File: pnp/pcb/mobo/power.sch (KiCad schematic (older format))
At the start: 27 parts, among them J45 Jack-DC, U14 FDS4435BZ, U5 AP1117-33, U7 TPS54336ADDA

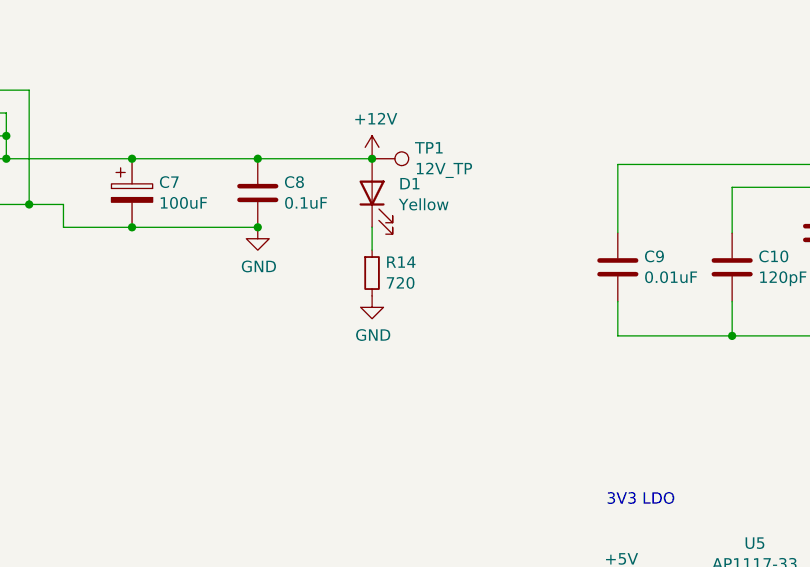
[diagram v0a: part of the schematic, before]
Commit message: - Fixing LED JLCPCB code to be a yellow LED as well as updating R14 to be 680R per Issue #99 - Updates to the schematic to include LCSC and JLC part numbers. - Updates to generate renders of the board as well as an HTML BOM with digikey links, and a JLCPCB BOM.
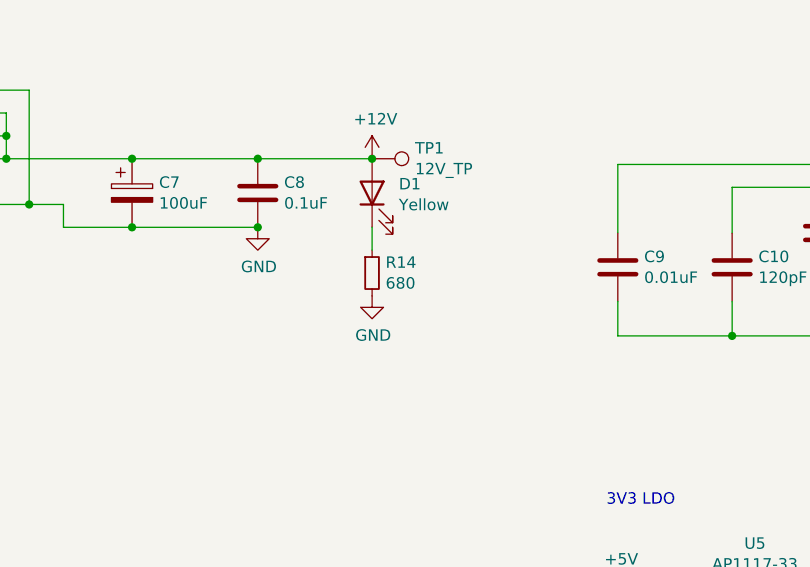
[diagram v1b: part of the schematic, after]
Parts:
- C10: Digikey (none) -> 399-1124-1-ND; JLCPCB (none) -> C159770; LCSC (none) -> C237175; Mouser (none) -> 80-C0805C121J5GAUTO
- C11, C9: Digikey (none) -> 1276-1015-1-ND; JLCPCB (none) -> C1710; LCSC (none) -> C83170; Mouser (none) -> 581-08055C104K
- C12, C29, C31, C8: Digikey (none) -> 1276-1180-1-ND; JLCPCB (none) -> C49678; LCSC (none) -> C360619; Mouser (none) -> 581-08055C104K
- C13, C30, C7: Digikey (none) -> 493-2203-1-ND; JLCPCB (none) -> C99837; LCSC (none) -> C263958; Mouser (none) -> 647-UWT1V101MCL1S
- D1, D2, D5: Digikey (none) -> 732-4987-1-ND; JLCPCB (none) -> C2296; LCSC (none) -> C779458; Mouser (none) -> 710-150080YS75000
- J45: LCSC (none) -> C16214
- L1: Digikey (none) -> SRR1260A-150MCT-ND; JLCPCB (none) -> C169395; LCSC (none) -> C397802; Mouser (none) -> 652-SRR1260A-150M
- R14: value 720 -> 680; JLCPCB (none) -> C17798; LCSC (none) -> C139848
- R15: Digikey (none) -> A129755CT-ND; JLCPCB (none) -> C26010; LCSC (none) -> C702834; Mouser (none) -> 71-CRCW08053K30FKEAC
- R16: Digikey (none) -> A129763CT-ND; JLCPCB (none) -> C17475; LCSC (none) -> C343944; Mouser (none) -> 71-RCG080515K0FKEA
- R17: Digikey (none) -> A129754CT-ND; JLCPCB (none) -> C17530; LCSC (none) -> C26019; Mouser (none) -> 652-CR0805FX-2701ELF
- R18: Digikey (none) -> A126343CT-ND; JLCPCB (none) -> C25270; LCSC (none) -> C294691; Mouser (none) -> 71-CRCW0805180RFKEA
- R42: Digikey (none) -> A129745CT-ND; JLCPCB (none) -> C17710; LCSC (none) -> C119076; Mouser (none) -> 71-CRCW0805470RFKEAC
- U14: JLCPCB (none) -> C23931; LCSC (none) -> C23931
- U5: JLCPCB (none) -> C108785; LCSC (none) -> C108785
- U7: Digikey (none) -> 296-43619-1-ND; JLCPCB (none) -> C97668; LCSC (none) -> C97668; Mouser (none) -> 595-TPS54336ADDAR
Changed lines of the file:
@@
 F 2 "Package_SO:TI_SO-PowerPAD-8_ThermalVias" H 8125 1325 50  0001 C CNN
 F 3 "http://www.ti.com/lit/ds/symlink/tps54336a.pdf" H 8225 1225 50  0001 C CNN
+F 4 "296-43619-1-ND" H 7225 1675 50  0001 C CNN "Digikey"
+F 5 "C97668" H 7225 1675 50  0001 C CNN "LCSC"
+F 6 "595-TPS54336ADDAR" H 7225 1675 50  0001 C CNN "Mouser"
+F 7 "C97668" H 7225 1675 50  0001 C CNN "JLCPCB"
 	1    7225 1675
 	1    0    0    -1
@@
 F 2 "Capacitor_SMD:CP_Elec_6.3x7.7" H 3488 1750 50  0001 C CNN
 F 3 "~" H 3450 1900 50  0001 C CNN
+F 4 "493-2203-1-ND" H 3450 1900 50  0001 C CNN "Digikey"
+F 5 "C263958" H 3450 1900 50  0001 C CNN "LCSC"
+F 6 "647-UWT1V101MCL1S" H 3450 1900 50  0001 C CNN "Mouser"
+F 7 "C99837" H 3450 1900 50  0001 C CNN "JLCPCB"
 	1    3450 1900
 	1    0    0    -1
@@
 F 2 "Capacitor_SMD:C_0805_2012Metric_Pad1.15x1.40mm_HandSolder" H 4038 1750 50  0001 C CNN
 F 3 "~" H 4000 1900 50  0001 C CNN
+F 4 "1276-1180-1-ND" H 4000 1900 50  0001 C CNN "Digikey"
+F 5 "C360619" H 4000 1900 50  0001 C CNN "LCSC"
+F 6 "581-08055C104K" H 4000 1900 50  0001 C CNN "Mouser"
+F 7 "C49678" H 4000 1900 50  0001 C CNN "JLCPCB"
 	1    4000 1900
 	1    0    0    -1
@@
 F 1 "15uH" H 8275 1799 50  0000 C CNN
 F 2 "Inductor_SMD:L_Bourns_SRR1260" H 8275 1675 50  0001 C CNN
-F 3 "~" H 8275 1675 50  0001 C CNN
+F 3 "https://www.bourns.com/docs/Product-Datasheets/SRR1260A.pdf" H 8275 1675 50  0001 C CNN
+F 4 "SRR1260A-150MCT-ND" H 8275 1675 50  0001 C CNN "Digikey"
+F 5 "C397802" H 8275 1675 50  0001 C CNN "LCSC"
+F 6 "652-SRR1260A-150M" H 8275 1675 50  0001 C CNN "Mouser"
+F 7 "C169395" H 8275 1675 50  0001 C CNN "JLCPCB"
 	1    8275 1675
 	1    0    0    -1
@@
 F 2 "Capacitor_SMD:C_0805_2012Metric_Pad1.15x1.40mm_HandSolder" H 7913 1325 50  0001 C CNN
 F 3 "~" H 7875 1475 50  0001 C CNN
+F 4 "1276-1180-1-ND" H 7875 1475 50  0001 C CNN "Digikey"
+F 5 "C360619" H 7875 1475 50  0001 C CNN "LCSC"
+F 6 "581-08055C104K" H 7875 1475 50  0001 C CNN "Mouser"
+F 7 "C49678" H 7875 1475 50  0001 C CNN "JLCPCB"
 	1    7875 1475
 	0    1    1    0
@@
 F 2 "Capacitor_SMD:C_0805_2012Metric_Pad1.15x1.40mm_HandSolder" H 6513 1925 50  0001 C CNN
 F 3 "~" H 6475 2075 50  0001 C CNN
+F 4 "1276-1015-1-ND" H 6475 2075 50  0001 C CNN "Digikey"
+F 5 "C83170" H 6475 2075 50  0001 C CNN "LCSC"
+F 6 "581-08055C104K" H 6475 2075 50  0001 C CNN "Mouser"
+F 7 "C1710" H 6475 2075 50  0001 C CNN "JLCPCB"
 	1    6475 2075
 	-1   0    0    1
@@
 F 2 "Resistor_SMD:R_0805_2012Metric_Pad1.15x1.40mm_HandSolder" H 6475 2375 50  0001 C CNN
 F 3 "~" H 6475 2375 50  0001 C CNN
+F 4 "A129755CT-ND" H 6475 2375 50  0001 C CNN "Digikey"
+F 5 "C702834" H 6475 2375 50  0001 C CNN "LCSC"
+F 6 "71-CRCW08053K30FKEAC" H 6475 2375 50  0001 C CNN "Mouser"
+F 7 "C26010" H 6475 2375 50  0001 C CNN "JLCPCB"
 	1    6475 2375
 	1    0    0    -1
@@
 F 2 "Capacitor_SMD:C_0805_2012Metric_Pad1.15x1.40mm_HandSolder" H 6113 2075 50  0001 C CNN
 F 3 "~" H 6075 2225 50  0001 C CNN
+F 4 "399-1124-1-ND" H 6075 2225 50  0001 C CNN "Digikey"
+F 5 "C237175" H 6075 2225 50  0001 C CNN "LCSC"
+F 6 "80-C0805C121J5GAUTO" H 6075 2225 50  0001 C CNN "Mouser"
+F 7 "C159770" H 6075 2225 50  0001 C CNN "JLCPCB"
 	1    6075 2225
 	-1   0    0    1
@@
 F 2 "Capacitor_SMD:C_0805_2012Metric_Pad1.15x1.40mm_HandSolder" H 5613 2075 50  0001 C CNN
 F 3 "~" H 5575 2225 50  0001 C CNN
+F 4 "1276-1015-1-ND" H 5575 2225 50  0001 C CNN "Digikey"
+F 5 "C83170" H 5575 2225 50  0001 C CNN "LCSC"
+F 6 "581-08055C104K" H 5575 2225 50  0001 C CNN "Mouser"
+F 7 "C1710" H 5575 2225 50  0001 C CNN "JLCPCB"
 	1    5575 2225
 	-1   0    0    1
@@
 F 2 "Capacitor_SMD:CP_Elec_6.3x7.7" H 8713 1675 50  0001 C CNN
 F 3 "~" H 8675 1825 50  0001 C CNN
+F 4 "493-2203-1-ND" H 8675 1825 50  0001 C CNN "Digikey"
+F 5 "C263958" H 8675 1825 50  0001 C CNN "LCSC"
+F 6 "647-UWT1V101MCL1S" H 8675 1825 50  0001 C CNN "Mouser"
+F 7 "C99837" H 8675 1825 50  0001 C CNN "JLCPCB"
 	1    8675 1825
 	1    0    0    -1
@@
 F 2 "Connector_BarrelJack:BarrelJack_Horizontal" H 1600 1810 50  0001 C CNN
 F 3 "~" H 1600 1810 50  0001 C CNN
+F 4 "C16214" H 1550 1850 50  0001 C CNN "LCSC"
 	1    1550 1850
 	1    0    0    -1
@@
 F 2 "LED_SMD:LED_0805_2012Metric" H 10075 1925 50  0001 C CNN
 F 3 "~" H 10075 1925 50  0001 C CNN
+F 4 "732-4987-1-ND" H 10075 1925 50  0001 C CNN "Digikey"
+F 5 "C779458" H 10075 1925 50  0001 C CNN "LCSC"
+F 6 "710-150080YS75000" H 10075 1925 50  0001 C CNN "Mouser"
+F 7 "C2296" H 10075 1925 50  0001 C CNN "JLCPCB"
 	1    10075 1925
 	0    -1   -1   0
@@
 F 2 "Resistor_SMD:R_0805_2012Metric_Pad1.15x1.40mm_HandSolder" H 10075 2275 50  0001 C CNN
 F 3 "~" H 10075 2275 50  0001 C CNN
+F 4 "A129745CT-ND" H 10075 2275 50  0001 C CNN "Digikey"
+F 5 "C119076" H 10075 2275 50  0001 C CNN "LCSC"
+F 6 "71-CRCW0805470RFKEAC" H 10075 2275 50  0001 C CNN "Mouser"
+F 7 "C17710" H 10075 2275 50  0001 C CNN "JLCPCB"
 	1    10075 2275
 	1    0    0    -1
@@
 F 2 "Resistor_SMD:R_0805_2012Metric_Pad1.15x1.40mm_HandSolder" H 9575 2425 50  0001 C CNN
 F 3 "~" H 9575 2425 50  0001 C CNN
+F 4 "A129754CT-ND" H 9575 2425 50  0001 C CNN "Digikey"
+F 5 "C26019" H 9575 2425 50  0001 C CNN "LCSC"
+F 6 "652-CR0805FX-2701ELF" H 9575 2425 50  0001 C CNN "Mouser"
+F 7 "C17530" H 9575 2425 50  0001 C CNN "JLCPCB"
 	1    9575 2425
 	1    0    0    -1
@@
 F 2 "Resistor_SMD:R_0805_2012Metric_Pad1.15x1.40mm_HandSolder" H 9575 2125 50  0001 C CNN
 F 3 "~" H 9575 2125 50  0001 C CNN
+F 4 "A129763CT-ND" H 9575 2125 50  0001 C CNN "Digikey"
+F 5 "C343944" H 9575 2125 50  0001 C CNN "LCSC"
+F 6 "71-RCG080515K0FKEA" H 9575 2125 50  0001 C CNN "Mouser"
+F 7 "C17475" H 9575 2125 50  0001 C CNN "JLCPCB"
 	1    9575 2125
 	1    0    0    -1
@@
 F 2 "Package_TO_SOT_SMD:SOT-223-3_TabPin2" H 6175 3875 50  0001 C CNN
 F 3 "http://www.diodes.com/datasheets/AP1117.pdf" H 6275 3425 50  0001 C CNN
+F 4 "C108785" H 6175 3675 50  0001 C CNN "JLCPCB"
+F 5 "C108785" H 6175 3675 50  0001 C CNN "LCSC"
 	1    6175 3675
 	1    0    0    -1
@@
 F 2 "Capacitor_SMD:C_0805_2012Metric_Pad1.15x1.40mm_HandSolder" H 9213 1675 50  0001 C CNN
 F 3 "~" H 9175 1825 50  0001 C CNN
+F 4 "1276-1180-1-ND" H 9175 1825 50  0001 C CNN "Digikey"
+F 5 "C360619" H 9175 1825 50  0001 C CNN "LCSC"
+F 6 "581-08055C104K" H 9175 1825 50  0001 C CNN "Mouser"
+F 7 "C49678" H 9175 1825 50  0001 C CNN "JLCPCB"
 	1    9175 1825
 	1    0    0    -1
@@
 F 2 "Capacitor_SMD:CP_Elec_6.3x7.7" H 7113 3675 50  0001 C CNN
 F 3 "~" H 7075 3825 50  0001 C CNN
+F 4 "493-2203-1-ND" H 7075 3825 50  0001 C CNN "Digikey"
+F 5 "C263958" H 7075 3825 50  0001 C CNN "LCSC"
+F 6 "647-UWT1V101MCL1S" H 7075 3825 50  0001 C CNN "Mouser"
+F 7 "C99837" H 7075 3825 50  0001 C CNN "JLCPCB"
 	1    7075 3825
 	1    0    0    -1
@@
 F 2 "Capacitor_SMD:C_0805_2012Metric_Pad1.15x1.40mm_HandSolder" H 6663 3675 50  0001 C CNN
 F 3 "~" H 6625 3825 50  0001 C CNN
+F 4 "1276-1180-1-ND" H 6625 3825 50  0001 C CNN "Digikey"
+F 5 "C360619" H 6625 3825 50  0001 C CNN "LCSC"
+F 6 "581-08055C104K" H 6625 3825 50  0001 C CNN "Mouser"
+F 7 "C49678" H 6625 3825 50  0001 C CNN "JLCPCB"
 	1    6625 3825
 	1    0    0    -1
@@
 F 2 "LED_SMD:LED_0805_2012Metric" H 7650 3850 50  0001 C CNN
 F 3 "~" H 7650 3850 50  0001 C CNN
+F 4 "732-4987-1-ND" H 7650 3850 50  0001 C CNN "Digikey"
+F 5 "C779458" H 7650 3850 50  0001 C CNN "LCSC"
+F 6 "710-150080YS75000" H 7650 3850 50  0001 C CNN "Mouser"
+F 7 "C2296" H 7650 3850 50  0001 C CNN "JLCPCB"
 	1    7650 3850
 	0    -1   -1   0
@@
 F 2 "Resistor_SMD:R_0805_2012Metric_Pad1.15x1.40mm_HandSolder" H 7650 4200 50  0001 C CNN
 F 3 "~" H 7650 4200 50  0001 C CNN
+F 4 "A126343CT-ND" H 7650 4200 50  0001 C CNN "Digikey"
+F 5 "C294691" H 7650 4200 50  0001 C CNN "LCSC"
+F 6 "71-CRCW0805180RFKEA" H 7650 4200 50  0001 C CNN "Mouser"
+F 7 "C25270" H 7650 4200 50  0001 C CNN "JLCPCB"
 	1    7650 4200
 	1    0    0    -1
@@
 F 2 "LED_SMD:LED_0805_2012Metric" H 4500 1900 50  0001 C CNN
 F 3 "~" H 4500 1900 50  0001 C CNN
+F 4 "732-4987-1-ND" H 4500 1900 50  0001 C CNN "Digikey"
+F 5 "C779458" H 4500 1900 50  0001 C CNN "LCSC"
+F 6 "710-150080YS75000" H 4500 1900 50  0001 C CNN "Mouser"
+F 7 "C2296" H 4500 1900 50  0001 C CNN "JLCPCB"
 	1    4500 1900
 	0    -1   -1   0
@@
 P 4500 2250
 F 0 "R14" H 4559 2296 50  0000 L CNN
-F 1 "720" H 4559 2205 50  0000 L CNN
+F 1 "680" H 4559 2205 50  0000 L CNN
 F 2 "Resistor_SMD:R_0805_2012Metric_Pad1.15x1.40mm_HandSolder" H 4500 2250 50  0001 C CNN
 F 3 "~" H 4500 2250 50  0001 C CNN
+F 4 "C139848" H 4500 2250 50  0001 C CNN "LCSC"
+F 5 "C17798" H 4500 2250 50  0001 C CNN "JLCPCB"
 	1    4500 2250
 	1    0    0    -1
@@
 F 2 "Package_SO:SO-8_3.9x4.9mm_P1.27mm" H 2500 1600 50  0001 C CNN
 F 3 "" H 2500 1600 50  0001 C CNN
+F 4 "C23931" H 2500 1600 50  0001 C CNN "JLCPCB"
+F 5 "C23931" H 2500 1600 50  0001 C CNN "LCSC"
 	1    2500 1600
 	-1   0    0    1
